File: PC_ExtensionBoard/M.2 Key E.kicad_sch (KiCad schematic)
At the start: 17 parts, among them J100 Bus_M.2_2199230-2

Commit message: components placement R1
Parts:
- A4: footprint antmicro-footprints:Mech_M2_2230_H2.5mm -> PC_Components_1:Mech_M2_2230_H2.5mm; Author Antmicro -> (none); Public False -> (none)
- C79, C80, C81, C82: footprint antmicro-footprints:C_0603_1608Metric -> PC_Components_1:C_0603_1608Metric
- D15: footprint antmicro-footprints:LED_0603_1608Metric_G -> PC_Components_1:LED_0603_1608Metric_G; Author Antmicro -> (none); License Apache-2.0 -> (none); Manufacturer Lite-On -> (none)
- D16: footprint antmicro-footprints:LED_0603_1608Metric_G -> PC_Components_1:LED_0603_1608Metric_G; Author Antmicro -> (none); License Apache-2.0 -> (none); Manufacturer Lite-On -> (none); Public False -> (none)
- H3: footprint antmicro-footprints:Spacer_Drill3.7mm_H2.5mm_9774025151R -> PC_Components_1:Spacer_Drill3.7mm_H2.5mm_9774025151R; Author Antmicro -> (none); License Apache-2.0 -> (none)
- J100: footprint antmicro-footprints:Bus_M.2_Socket_Key_E_TE_2199230-6 -> PC_Components_1:Bus_M.2_Socket_Key_E_TE_2199230-6; Author Antmicro -> (none); LCSC (none) -> C23731731; License Apache-2.0 -> (none); MPN 2199230-2 -> (none); Manufacturer TE Connectivity -> (none)
- R132, R135, R136: footprint antmicro-footprints:R_0402_1005Metric -> PC_Components_1:R_0402_1005Metric
- R133: footprint antmicro-footprints:R_0402_1005Metric -> PC_Components_1:R_0402_1005Metric; Author Antmicro -> (none); Manufacturer Panasonic -> (none); Public False -> (none)
- R134, R137: footprint antmicro-footprints:R_0402_1005Metric -> PC_Components_1:R_0402_1005Metric; Author Antmicro -> (none); License Apache-2.0 -> (none); Manufacturer Panasonic -> (none); Public False -> (none)
- R138, R139: footprint antmicro-footprints:R_0402_1005Metric -> PC_Components_1:R_0402_1005Metric; License Apache-2.0 -> (none); Manufacturer Bourns -> (none); Public False -> (none)

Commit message: refactor project
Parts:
- A4: symbol antmicroModules:Mech_M2_2230_H2.5mm -> A_PC_ExtensionBoard:Mech_M2_2230_H2.5mm
- C79, C80, C81, C82: symbol antmicroCapacitors0603:C_22u_16V_0603 -> A_PC_ExtensionBoard:C_22u_16V_0603
- D15: symbol antmicroLEDIndicationDiscrete:LED_G_0603_LTST-C190GKT -> A_PC_ExtensionBoard:LED_G_0603_LTST-C190GKT
- D16: symbol antmicroLEDIndicationDiscrete:LED_G_0603_LTST-C190GKT -> A_PC_ExtensionBoard:LED_G_0603_LTST-C190GKT; Public (none) -> False
- H3: symbol antmicroMechanicalParts:Spacer_Drill3.7mm_H2.5mm_9774025151R -> A_PC_ExtensionBoard:Spacer_Drill3.7mm_H2.5mm_9774025151R
- J100: symbol antmicroPciConnectors:Bus_M.2_2199230-2 -> A_PC_ExtensionBoard:Bus_M.2_2199230-2
- R132: footprint PC_Components_1:R_0402_1005Metric -> antmicro-footprints:R_0402_1005Metric; symbol antmicroResistors0402:R_0R_0402 -> A_PC_ExtensionBoard:R_0R_0402
- R133: footprint PC_Components_1:R_0402_1005Metric -> antmicro-footprints:R_0402_1005Metric; symbol antmicroResistors0402:R_0R_0402 -> A_PC_ExtensionBoard:R_0R_0402; Author (none) -> Antmicro; Manufacturer (none) -> Panasonic; Public (none) -> False
- R134, R137: footprint PC_Components_1:R_0402_1005Metric -> antmicro-footprints:R_0402_1005Metric; symbol antmicroResistors0402:R_0R_0402 -> A_PC_ExtensionBoard:R_0R_0402; Author (none) -> Antmicro; License (none) -> Apache-2.0; Manufacturer (none) -> Panasonic; Public (none) -> False
- R135, R136: footprint PC_Components_1:R_0402_1005Metric -> antmicro-footprints:R_0402_1005Metric; symbol antmicroResistors0402:R_10k_0402 -> A_PC_ExtensionBoard:R_10k_0402
- R138, R139: symbol antmicroResistors0402:R_220R_0402 -> A_PC_ExtensionBoard:R_220R_0402
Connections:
- net +3V3 renamed +3.3V
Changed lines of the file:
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@@
 	)
 	(symbol
-		(lib_id "antmicroResistors0402:R_220R_0402")
+		(lib_id "A_PC_ExtensionBoard:R_220R_0402")
 		(at 152.4 130.81 90)
 		(unit 1)
@@
 	)
 	(symbol
-		(lib_id "antmicropower:+3V3")
+		(lib_id "power:+3.3V")
 		(at 152.4 125.73 0)
 		(unit 1)
@@
 			)
 		)
-		(property "Value" "+3V3"
+		(property "Value" "+3.3V"
 			(at 152.4 121.92 0)
 			(show_name no)
@@
 	)
 	(symbol
-		(lib_id "antmicroResistors0402:R_0R_0402")
+		(lib_id "A_PC_ExtensionBoard:R_0R_0402")
 		(at 127 67.31 0)
 		(unit 1)
@@
 			)
 		)
-		(property "Footprint" "PC_Components_1:R_0402_1005Metric"
+		(property "Footprint" "antmicro-footprints:R_0402_1005Metric"
 			(at 147.32 82.55 0)
 			(hide yes)
@@
 			)
 		)
+		(property "Manufacturer" "Panasonic"
+			(at 147.32 90.17 0)
+			(hide yes)
+			(show_name no)
+			(do_not_autoplace no)
+			(effects
+				(font
+					(size 1.27 1.27)
+					(thickness 0.15)
+				)
+				(justify left bottom)
+			)
+		)
+		(property "License" "Apache-2.0"
+			(at 147.32 92.71 0)
+			(hide yes)
+			(show_name no)
+			(do_not_autoplace no)
+			(effects
+				(font
+					(size 1.27 1.27)
+					(thickness 0.15)
+				)
+				(justify left bottom)
+			)
+		)
+		(property "Author" "Antmicro"
+			(at 147.32 95.25 0)
+			(hide yes)
+			(show_name no)
+			(do_not_autoplace no)
+			(effects
+				(font
+					(size 1.27 1.27)
+					(thickness 0.15)
+				)
+				(justify left bottom)
+			)
+		)
+		(property "Public" "False"
+			(at 147.32 97.79 0)
+			(hide yes)
+			(show_name no)
+			(do_not_autoplace no)
+			(effects
+				(font
+					(size 1.27 1.27)
+				)
+				(justify left bottom)
+			)
+		)
 		(pin "1"
 		)
@@
 	)
 	(symbol
-		(lib_id "antmicropower:+3V3")
+		(lib_id "power:+3.3V")
 		(at 152.4 44.45 0)
 		(unit 1)
@@
 			)
 		)
-		(property "Value" "+3V3"
+		(property "Value" "+3.3V"
 			(at 152.4 40.64 0)
 			(show_name no)
@@
 	)
 	(symbol
-		(lib_id "antmicropower:+3V3")
+		(lib_id "power:+3.3V")
 		(at 139.7 125.73 0)
 		(unit 1)
@@
 			)
 		)
-		(property "Value" "+3V3"
+		(property "Value" "+3.3V"
 			(at 139.7 121.92 0)
 			(show_name no)
@@
 	)
 	(symbol
-		(lib_id "antmicropower:GND")
+		(lib_id "power:GND")
 		(at 152.4 55.88 0)
 		(unit 1)
@@
 	)
 	(symbol
-		(lib_id "antmicroCapacitors0603:C_22u_16V_0603")
+		(lib_id "A_PC_ExtensionBoard:C_22u_16V_0603")
 		(at 152.4 54.61 90)
 		(unit 1)
@@
 	)
 	(symbol
-		(lib_id "antmicroResistors0402:R_10k_0402")
+		(lib_id "A_PC_ExtensionBoard:R_10k_0402")
 		(at 71.12 53.34 90)
 		(unit 1)
@@
 			)
 		)
-		(property "Footprint" "PC_Components_1:R_0402_1005Metric"
+		(property "Footprint" "antmicro-footprints:R_0402_1005Metric"
 			(at 86.36 33.02 0)
 			(hide yes)
@@
 	)
 	(symbol
-		(lib_id "antmicroCapacitors0603:C_22u_16V_0603")
+		(lib_id "A_PC_ExtensionBoard:C_22u_16V_0603")
 		(at 125.73 54.61 90)
 		(unit 1)
@@
 	)
 	(symbol
-		(lib_id "antmicroResistors0402:R_0R_0402")
+		(lib_id "A_PC_ExtensionBoard:R_0R_0402")
 		(at 59.69 135.89 0)
 		(unit 1)
@@
 			)
 		)
-		(property "Footprint" "PC_Components_1:R_0402_1005Metric"
+		(property "Footprint" "antmicro-footprints:R_0402_1005Metric"
 			(at 80.01 151.13 0)
 			(hide yes)
@@
 			)
 		)
+		(property "Manufacturer" "Panasonic"
+			(at 80.01 158.75 0)
+			(hide yes)
+			(show_name no)
+			(do_not_autoplace no)
+			(effects
+				(font
+					(size 1.27 1.27)
+					(thickness 0.15)
+				)
+				(justify left bottom)
+			)
+		)
+		(property "License" "Apache-2.0"
+			(at 80.01 161.29 0)
+			(hide yes)
+			(show_name no)
+			(do_not_autoplace no)
+			(effects
+				(font
+					(size 1.27 1.27)
+					(thickness 0.15)
+				)
+				(justify left bottom)
+			)
+		)
+		(property "Author" "Antmicro"
+			(at 80.01 163.83 0)
+			(hide yes)
+			(show_name no)
+			(do_not_autoplace no)
+			(effects
+				(font
+					(size 1.27 1.27)
+					(thickness 0.15)
+				)
+				(justify left bottom)
+			)
+		)
+		(property "Public" "False"
+			(at 80.01 166.37 0)
+			(hide yes)
+			(show_name no)
+			(do_not_autoplace no)
+			(effects
+				(font
+					(size 1.27 1.27)
+				)
+				(justify left bottom)
+			)
+		)
 		(pin "1"
 		)
@@
 	)
 	(symbol
-		(lib_id "antmicroResistors0402:R_0R_0402")
+		(lib_id "A_PC_ExtensionBoard:R_0R_0402")
 		(at 49.53 54.61 0)
 		(unit 1)
@@
 			)
 		)
-		(property "Footprint" "PC_Components_1:R_0402_1005Metric"
+		(property "Footprint" "antmicro-footprints:R_0402_1005Metric"
 			(at 69.85 69.85 0)
 			(hide yes)
@@
 	)
 	(symbol
-		(lib_id "antmicropower:GND")
+		(lib_id "power:GND")
 		(at 123.19 160.02 0)
 		(unit 1)
@@
 	)
 	(symbol
-		(lib_id "antmicroResistors0402:R_220R_0402")
+		(lib_id "A_PC_ExtensionBoard:R_220R_0402")
 		(at 139.7 130.81 90)
 		(unit 1)
@@
 	)
 	(symbol
-		(lib_id "antmicroResistors0402:R_10k_0402")
+		(lib_id "A_PC_ExtensionBoard:R_10k_0402")
 		(at 80.01 53.34 90)
 		(unit 1)
@@
 			)
 		)
-		(property "Footprint" "PC_Components_1:R_0402_1005Metric"
+		(property "Footprint" "antmicro-footprints:R_0402_1005Metric"
 			(at 95.25 33.02 0)
 			(hide yes)
@@
 	)
 	(symbol
-		(lib_id "antmicropower:GND")
+		(lib_id "power:GND")
 		(at 134.62 55.88 0)
 		(unit 1)
@@
 	)
 	(symbol
-		(lib_id "antmicroModules:Mech_M2_2230_H2.5mm")
+		(lib_id "A_PC_ExtensionBoard:Mech_M2_2230_H2.5mm")
 		(at 182.88 118.11 0)
 		(unit 1)
@@
 	)
 	(symbol
-		(lib_id "antmicroCapacitors0603:C_22u_16V_0603")
+		(lib_id "A_PC_ExtensionBoard:C_22u_16V_0603")
 		(at 143.51 54.61 90)
 		(unit 1)
@@
 	)
 	(symbol
-		(lib_id "antmicroResistors0402:R_0R_0402")
+		(lib_id "A_PC_ExtensionBoard:R_0R_0402")
 		(at 59.69 133.35 0)
 		(unit 1)
@@
 			)
 		)
-		(property "Footprint" "PC_Components_1:R_0402_1005Metric"
+		(property "Footprint" "antmicro-footprints:R_0402_1005Metric"
 			(at 80.01 148.59 0)
 			(hide yes)
@@
 			)
 		)
+		(property "Manufacturer" "Panasonic"
+			(at 80.01 156.21 0)
+			(hide yes)
+			(show_name no)
+			(do_not_autoplace no)
+			(effects
+				(font
+					(size 1.27 1.27)
+					(thickness 0.15)
+				)
+				(justify left bottom)
+			)
+		)
+		(property "Author" "Antmicro"
+			(at 80.01 161.29 0)
+			(hide yes)
+			(show_name no)
+			(do_not_autoplace no)
+			(effects
+				(font
+					(size 1.27 1.27)
+					(thickness 0.15)
+				)
+				(justify left bottom)
+			)
+		)
+		(property "Public" "False"
+			(at 80.01 163.83 0)
+			(hide yes)
+			(show_name no)
+			(do_not_autoplace no)
+			(effects
+				(font
+					(size 1.27 1.27)
+				)
+				(justify left bottom)
+			)
+		)
 		(pin "1"
 		)
@@
 	)
 	(symbol
-		(lib_id "antmicropower:+3V3")
+		(lib_id "power:+3.3V")
 		(at 71.12 45.72 0)
 		(unit 1)
@@
 			)
 		)
-		(property "Value" "+3V3"
+		(property "Value" "+3.3V"
 			(at 71.12 42.164 0)
 			(show_name no)
@@
 	)
 	(symbol
-		(lib_id "antmicropower:GND")
+		(lib_id "power:GND")
 		(at 181.61 132.08 0)
 		(unit 1)
@@
 	)
 	(symbol
-		(lib_id "antmicropower:GND")
+		(lib_id "power:GND")
 		(at 125.73 55.88 0)
 		(unit 1)
@@
 	)
 	(symbol
-		(lib_id "antmicroLEDIndicationDiscrete:LED_G_0603_LTST-C190GKT")
+		(lib_id "A_PC_ExtensionBoard:LED_G_0603_LTST-C190GKT")
 		(at 139.7 137.16 90)
 		(unit 1)
@@
 	)
 	(symbol
-		(lib_id "antmicroMechanicalParts:Spacer_Drill3.7mm_H2.5mm_9774025151R")
+		(lib_id "A_PC_ExtensionBoard:Spacer_Drill3.7mm_H2.5mm_9774025151R")
 		(at 182.88 130.81 0)
 		(mirror x)
@@
 	)
 	(symbol
-		(lib_id "antmicroLEDIndicationDiscrete:LED_G_0603_LTST-C190GKT")
+		(lib_id "A_PC_ExtensionBoard:LED_G_0603_LTST-C190GKT")
 		(at 152.4 137.16 90)
 		(unit 1)
@@
 			)
 		)
+		(property "Public" "False"
+			(at 170.18 116.84 0)
+			(hide yes)
+			(show_name no)
+			(do_not_autoplace no)
+			(effects
+				(font
+					(size 1.27 1.27)
+				)
+				(justify left bottom)
+			)
+		)
 		(pin "1"
 		)
@@
 	)
 	(symbol
-		(lib_id "antmicroPciConnectors:Bus_M.2_2199230-2")
+		(lib_id "A_PC_ExtensionBoard:Bus_M.2_2199230-2")
 		(at 87.63 54.61 0)
 		(unit 1)
@@
 	)
 	(symbol
-		(lib_id "antmicroCapacitors0603:C_22u_16V_0603")
+		(lib_id "A_PC_ExtensionBoard:C_22u_16V_0603")
 		(at 134.62 54.61 90)
 		(unit 1)
@@
 	)
 	(symbol
-		(lib_id "antmicropower:GND")
+		(lib_id "power:GND")
 		(at 143.51 55.88 0)
 		(unit 1)

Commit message: re-link symbol
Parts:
- added U2: 10GHz, ACLAB:SMA-TH_SMA-KWE, symbol A_PC_ExtensionBoard:Antenna_SMA-KWE_C20415790_
- R132, R133, R134, R135, R136, R137: footprint antmicro-footprints:R_0402_1005Metric -> PC_Components_1:R_0402_1005Metric
- renumbered H3 to H11

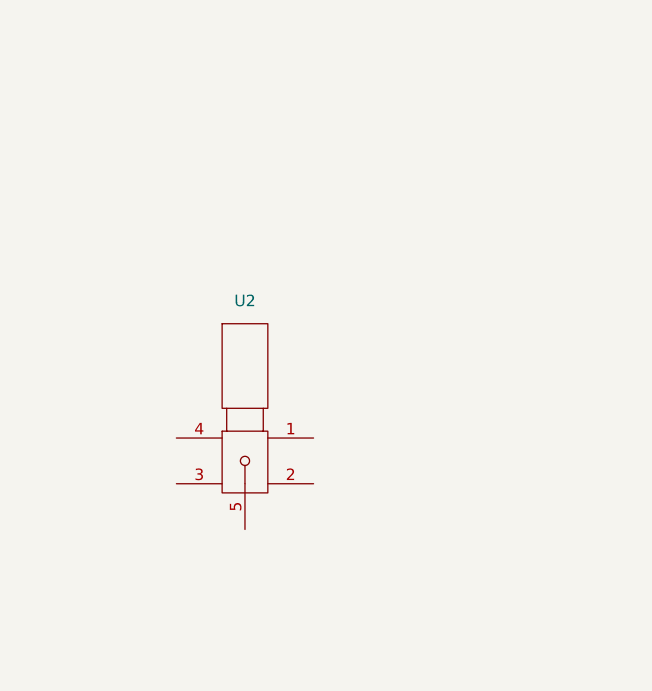
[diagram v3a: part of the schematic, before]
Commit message: update LCSC for HDMI
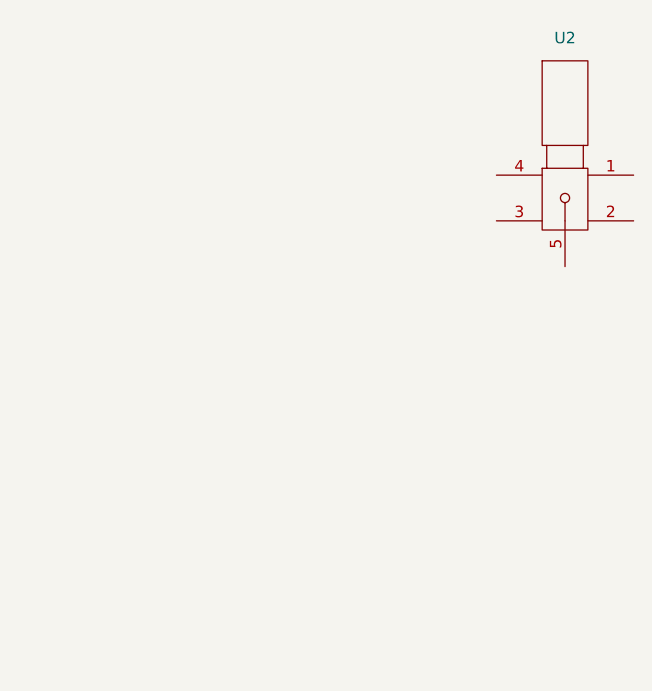
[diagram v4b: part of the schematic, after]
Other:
- moved on the sheet: U2
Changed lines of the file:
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@@
 	(symbol
 		(lib_id "A_PC_ExtensionBoard:Antenna_SMA-KWE_C20415790_")
-		(at 238.76 64.77 0)
+		(at 274.32 35.56 0)
 		(unit 1)
 		(body_style 1)
@@
 		(fields_autoplaced yes)
 		(property "Reference" "U2"
-			(at 238.76 49.53 0)
+			(at 274.32 20.32 0)
 			(show_name no)
 			(do_not_autoplace no)
@@
 		)
 		(property "Value" "10GHz"
-			(at 238.76 64.77 90)
+			(at 274.32 35.56 90)
 			(hide yes)
 			(show_name no)
@@
 		)
 		(property "Footprint" "ACLAB:SMA-TH_SMA-KWE"
-			(at 238.76 64.77 0)
+			(at 274.32 35.56 0)
 			(hide yes)
 			(show_name no)
@@
 		)
 		(property "Datasheet" "https://item.szlcsc.com/datasheet/SMA-KWE/21743972.html"
-			(at 238.76 64.77 90)
+			(at 274.32 35.56 90)
 			(hide yes)
 			(show_name no)
@@
 		)
 		(property "Description" ""
-			(at 238.76 64.77 0)
+			(at 274.32 35.56 0)
 			(hide yes)
 			(show_name no)
@@
 		)
 		(property "SYMBOL" "SMA-KWE_C20415790"
-			(at 238.76 64.77 90)
+			(at 274.32 35.56 90)
 			(hide yes)
 			(show_name no)
@@
 		)
 		(property "DEVICE" "SMA-KWE_C20415790"
-			(at 238.76 64.77 90)
+			(at 274.32 35.56 90)
 			(hide yes)
 			(show_name no)
@@
 		)
 		(property "LCSC PART NAME" "内孔 SMA 弯头"
-			(at 238.76 64.77 90)
+			(at 274.32 35.56 90)
 			(hide yes)
 			(show_name no)
@@
 		)
 		(property "SUPPLIER PART" "C20415790"
-			(at 238.76 64.77 90)
+			(at 274.32 35.56 90)
 			(hide yes)
 			(show_name no)
@@
 		)
 		(property "MANUFACTURER" "cntitle(中戈泰斗)"
-			(at 238.76 64.77 90)
+			(at 274.32 35.56 90)
 			(hide yes)
 			(show_name no)
@@
 		)
 		(property "MANUFACTURER PART" "SMA-KWE"
-			(at 238.76 64.77 90)
+			(at 274.32 35.56 90)
 			(hide yes)
 			(show_name no)
@@
 		)
 		(property "SUPPLIER FOOTPRINT" "弯插"
-			(at 238.76 64.77 90)
+			(at 274.32 35.56 90)
 			(hide yes)
 			(show_name no)
@@
 		)
 		(property "JLCPCB PART CLASS" "Extended Part"
-			(at 238.76 64.77 90)
+			(at 274.32 35.56 90)
 			(hide yes)
 			(show_name no)
@@
 		)
 		(property "SUPPLIER" "LCSC"
-			(at 238.76 64.77 90)
+			(at 274.32 35.56 90)
 			(hide yes)
 			(show_name no)
@@
 		)
 		(property "ADD INTO BOM" "yes"
-			(at 238.76 64.77 90)
+			(at 274.32 35.56 90)
 			(hide yes)
 			(show_name no)
@@
 		)
 		(property "CONVERT TO PCB" "yes"
-			(at 238.76 64.77 90)
+			(at 274.32 35.56 90)
 			(hide yes)
 			(show_name no)
@@
 		)
 		(property "CONNECTOR TYPE" "Board Side"
-			(at 238.76 64.77 90)
+			(at 274.32 35.56 90)
 			(hide yes)
 			(show_name no)
@@
 		)
 		(property "INTERFACE" "Inner Bore"
-			(at 238.76 64.77 90)
+			(at 274.32 35.56 90)
 			(hide yes)
 			(show_name no)
@@
 		)
 		(property "NUMBER OF PORTS" "1"
-			(at 238.76 64.77 90)
+			(at 274.32 35.56 90)
 			(hide yes)
 			(show_name no)
@@
 		)
 		(property "INTERFACE LENGTH/HEIGHT" "7.8mm"
-			(at 238.76 64.77 90)
+			(at 274.32 35.56 90)
 			(hide yes)
 			(show_name no)
@@
 		)
 		(property "ALTIUM_VALUE" "10GHz"
-			(at 238.76 64.77 90)
+			(at 274.32 35.56 90)
 			(hide yes)
 			(show_name no)
@@
 		)
 		(property "RF SERIES" "SMA"
-			(at 238.76 64.77 90)
+			(at 274.32 35.56 90)
 			(hide yes)
 			(show_name no)
@@
 		)
 		(property "IMPEDANCE" "50Ω"
-			(at 238.76 64.77 90)
+			(at 274.32 35.56 90)
 			(hide yes)
 			(show_name no)
@@
 		)
 		(property "STYLE" "Elbow"
-			(at 238.76 64.77 90)
-			(hide yes)
-			(show_name no)
+			(at 274.32 35.56 90)
+			(hide yes)
+			(show_name no)

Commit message: update LCSC Number
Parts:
- R132, R133: LCSC (none) -> C242160
- R134, R137: Author Antmicro -> (none); Current 1A -> (none); LCSC (none) -> C242160; License Apache-2.0 -> (none); Manufacturer Panasonic -> (none); Public False -> (none)
- U2: LCSC (none) -> C7498154
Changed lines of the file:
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@@
 			)
 		)
-		(property "Tolerance" ""
-			(at 147.32 77.47 0)
-			(hide yes)
-			(show_name no)
-			(do_not_autoplace no)
-			(effects
-				(font
-					(size 1.27 1.27)
-				)
-				(justify left bottom)
-			)
-		)
-		(property "Current" "1A"
-			(at 129.54 63.5 0)
-			(hide yes)
-			(show_name no)
-			(do_not_autoplace no)
-			(effects
-				(font
-					(size 1.27 1.27)
-					(thickness 0.15)
-				)
-			)
-		)
-		(property "Manufacturer" "Panasonic"
-			(at 147.32 90.17 0)
-			(hide yes)
-			(show_name no)
-			(do_not_autoplace no)
-			(effects
-				(font
-					(size 1.27 1.27)
-					(thickness 0.15)
-				)
-				(justify left bottom)
-			)
-		)
-		(property "License" "Apache-2.0"
-			(at 147.32 92.71 0)
-			(hide yes)
-			(show_name no)
-			(do_not_autoplace no)
-			(effects
-				(font
-					(size 1.27 1.27)
-					(thickness 0.15)
-				)
-				(justify left bottom)
-			)
-		)
-		(property "Author" "Antmicro"
-			(at 147.32 95.25 0)
-			(hide yes)
-			(show_name no)
-			(do_not_autoplace no)
-			(effects
-				(font
-					(size 1.27 1.27)
-					(thickness 0.15)
-				)
-				(justify left bottom)
-			)
-		)
-		(property "Public" "False"
-			(at 147.32 97.79 0)
-			(hide yes)
-			(show_name no)
-			(do_not_autoplace no)
-			(effects
-				(font
-					(size 1.27 1.27)
-				)
-				(justify left bottom)
+		(property "LCSC" "C242160"
+			(at 127 67.31 0)
+			(hide yes)
+			(show_name no)
+			(do_not_autoplace no)
+			(effects
+				(font
+					(size 1.27 1.27)
+				)
 			)
 		)
@@
 			)
 		)
-		(property "Tolerance" ""
-			(at 80.01 146.05 0)
-			(hide yes)
-			(show_name no)
-			(do_not_autoplace no)
-			(effects
-				(font
-					(size 1.27 1.27)
-				)
-				(justify left bottom)
-			)
-		)
-		(property "Current" "1A"
-			(at 62.23 132.715 0)
-			(hide yes)
-			(show_name no)
-			(do_not_autoplace no)
-			(effects
-				(font
-					(size 1.27 1.27)
-					(thickness 0.15)
-				)
-			)
-		)
-		(property "Manufacturer" "Panasonic"
-			(at 80.01 158.75 0)
-			(hide yes)
-			(show_name no)
-			(do_not_autoplace no)
-			(effects
-				(font
-					(size 1.27 1.27)
-					(thickness 0.15)
-				)
-				(justify left bottom)
-			)
-		)
-		(property "License" "Apache-2.0"
-			(at 80.01 161.29 0)
-			(hide yes)
-			(show_name no)
-			(do_not_autoplace no)
-			(effects
-				(font
-					(size 1.27 1.27)
-					(thickness 0.15)
-				)
-				(justify left bottom)
-			)
-		)
-		(property "Author" "Antmicro"
-			(at 80.01 163.83 0)
-			(hide yes)
-			(show_name no)
-			(do_not_autoplace no)
-			(effects
-				(font
-					(size 1.27 1.27)
-					(thickness 0.15)
-				)
-				(justify left bottom)
-			)
-		)
-		(property "Public" "False"
-			(at 80.01 166.37 0)
-			(hide yes)
-			(show_name no)
-			(do_not_autoplace no)
-			(effects
-				(font
-					(size 1.27 1.27)
-				)
-				(justify left bottom)
+		(property "LCSC" "C242160"
+			(at 59.69 135.89 0)
+			(hide yes)
+			(show_name no)
+			(do_not_autoplace no)
+			(effects
+				(font
+					(size 1.27 1.27)
+				)
 			)
 		)
@@
 				)
 				(justify left bottom)
+			)
+		)
+		(property "LCSC" "C242160"
+			(at 49.53 54.61 0)
+			(hide yes)
+			(show_name no)
+			(do_not_autoplace no)
+			(effects
+				(font
+					(size 1.27 1.27)
+				)
 			)
 		)
@@
 			)
 		)
+		(property "LCSC" "C7498154"
+			(at 274.32 35.56 0)
+			(hide yes)
+			(show_name no)
+			(do_not_autoplace no)
+			(effects
+				(font
+					(size 1.27 1.27)
+				)
+			)
+		)
 		(pin "2"
 		)
@@
 			)
 		)
+		(property "LCSC" "C242160"
+			(at 59.69 133.35 0)
+			(hide yes)
+			(show_name no)
+			(do_not_autoplace no)
+			(effects
+				(font
+					(size 1.27 1.27)
+				)
+			)
+		)

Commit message: update Schematic
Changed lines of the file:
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@@
+	)
+	(no_connect
+		(at 62.23 92.71)
 	)
 	(no_connect
@@
 	)
 	(no_connect
+		(at 62.23 97.79)
+	)
+	(no_connect
+		(at 62.23 100.33)
+	)
+	(no_connect
 		(at 87.63 95.25)
 	)
@@
 	)
 	(no_connect
-		(at 62.23 100.33)
-	)
-	(no_connect
-		(at 62.23 97.79)
-	)
-	(no_connect
 		(at 118.11 97.79)
 	)
@@
 	)
 	(no_connect
+		(at 60.96 90.17)
+	)
+	(no_connect
 		(at 87.63 140.97)
 	)
@@
 	)
 	(no_connect
-		(at 62.23 90.17)
-	)
-	(no_connect
 		(at 118.11 123.19)
 	)
@@
 	(no_connect
 		(at 118.11 102.87)
-	)
-	(no_connect
-		(at 62.23 92.71)
 	)
 	(no_connect
@@
 	(wire
 		(pts
-			(xy 62.23 90.17) (xy 44.45 90.17)
+			(xy 60.96 90.17) (xy 44.45 90.17)
 		)
 		(stroke
@@
 	)
 	(label "PCIe_{x1}.TX1+"
-		(at 62.23 90.17 180)
+		(at 60.96 90.17 180)
 		(effects
 			(font
